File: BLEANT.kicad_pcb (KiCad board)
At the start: 4 copper layers, 75.8 x 76.2 mm, 71 parts, among them IC1 FAN4010IL6X_F113, IC2 FAN4010IL6X_F113, J1 Conn_01x04_Male, J2 SC_19-20, J3 Conn_01x02, J4 Conn_01x02, J5 1909763-1, U1 nRF51x22-QFxx, U2 LM50BIM3, U3 MP5077GG-Z, U4 MP5077GG-Z, U5 MCP2515-xSO, U6 SN65HVD1050D, X2 32.768kHz, Y1 16MHz

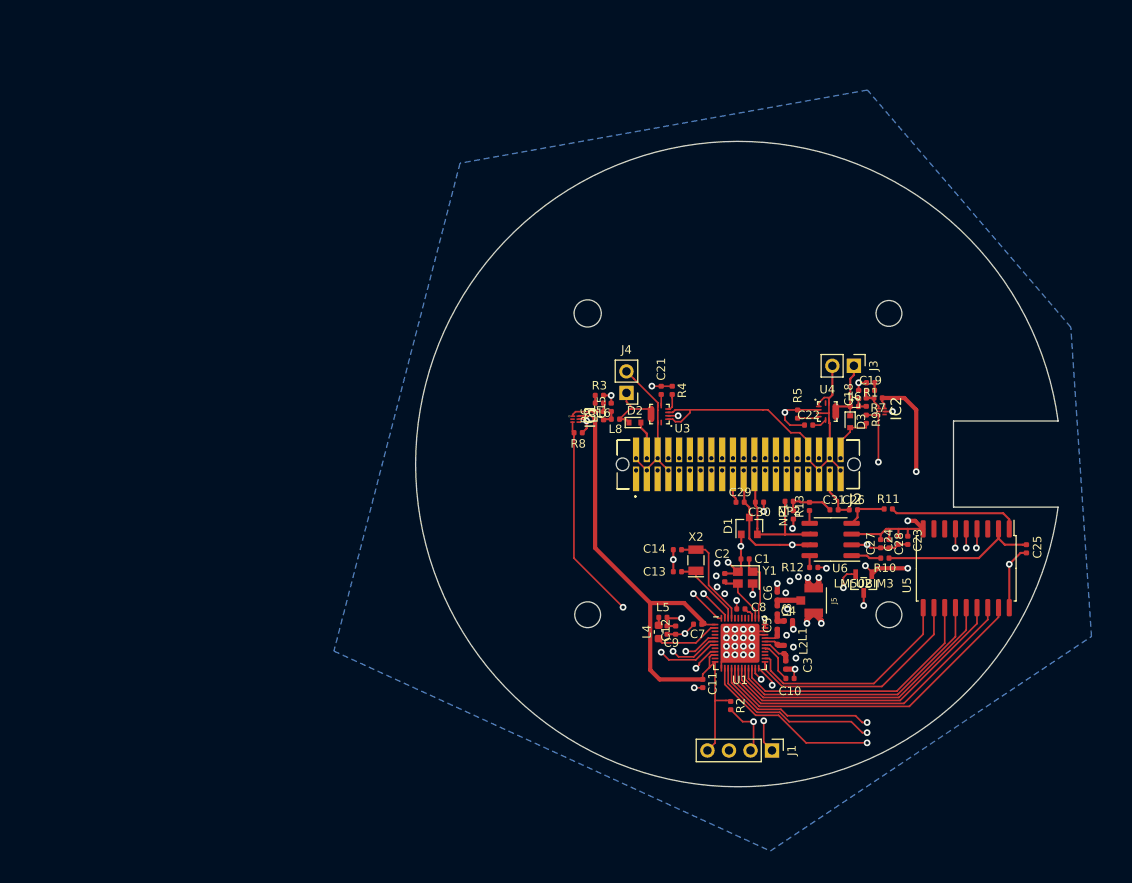
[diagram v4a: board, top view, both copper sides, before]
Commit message: Added ground pours and stitching vias
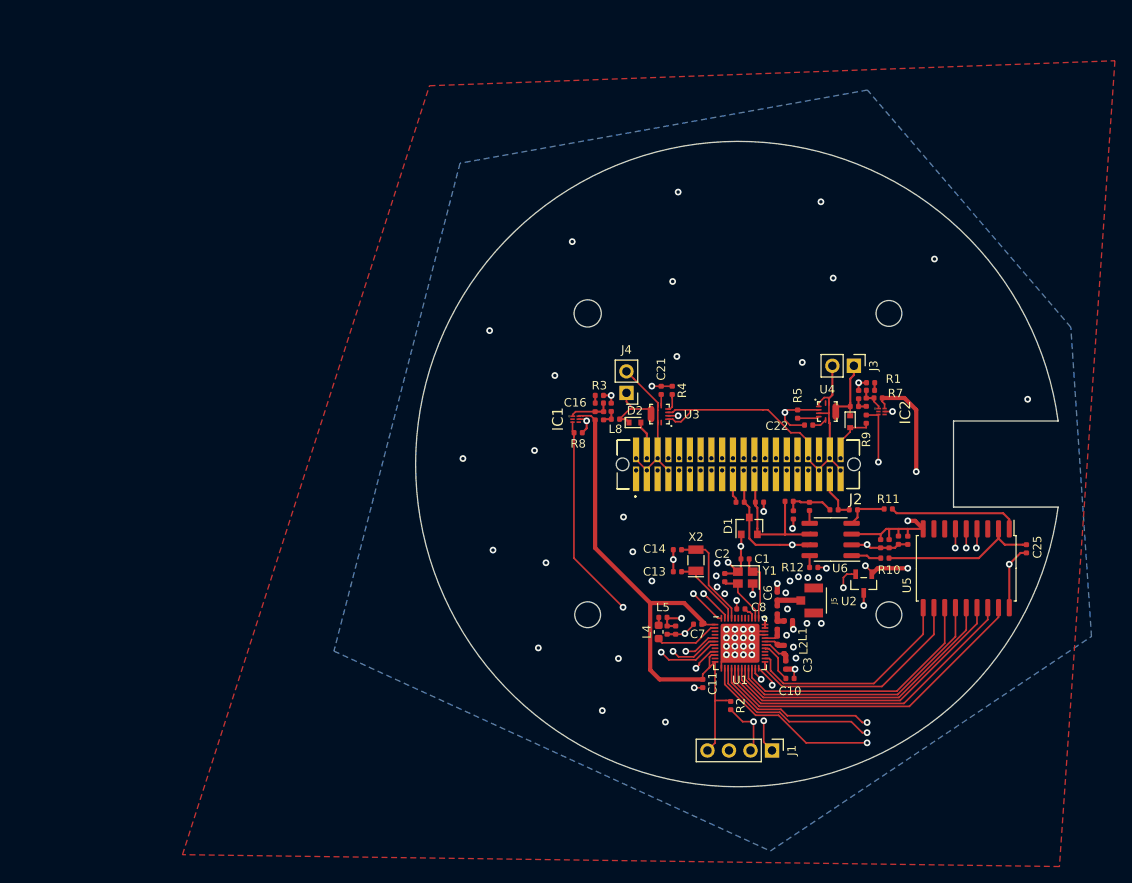
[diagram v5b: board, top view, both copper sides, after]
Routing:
- net GND: track 97.0 -> 90.9 mm, vias 53 -> 75
- added copper zone on F.Cu, net GND
- added copper zone on In2.Cu, net GND

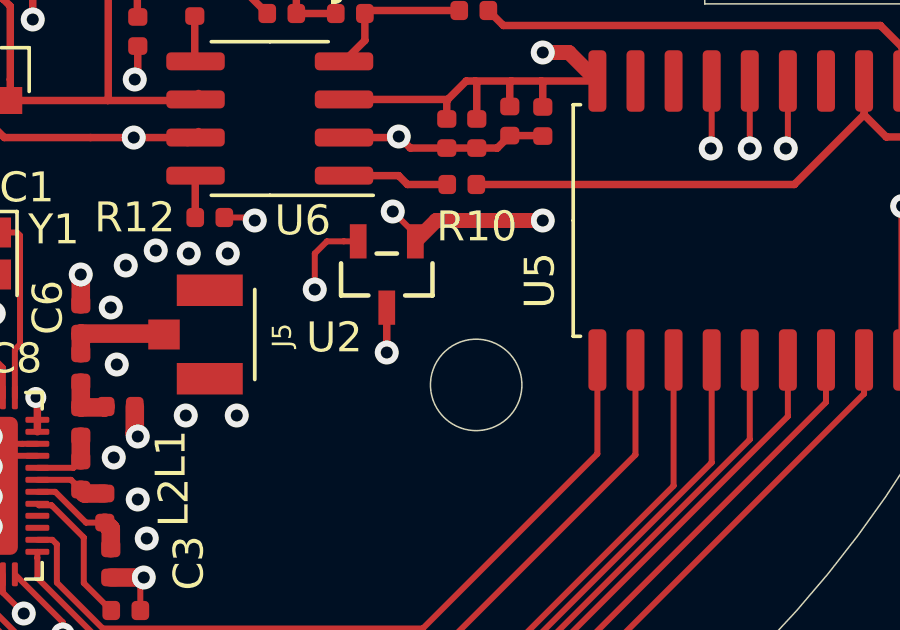
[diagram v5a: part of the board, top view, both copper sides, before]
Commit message: Made my chip not blow up with voltage dividers
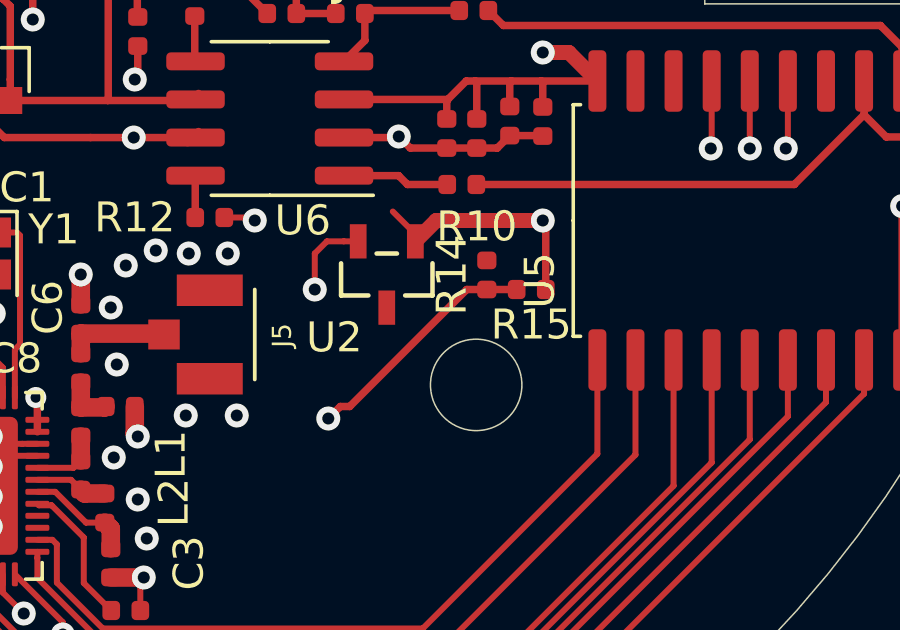
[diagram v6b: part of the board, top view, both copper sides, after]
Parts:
- added R14: 10k, Resistor_SMD:R_0402_1005Metric, F.Cu at (170.5, 141.1)
- added R15: 6k, Resistor_SMD:R_0402_1005Metric, F.Cu at (172.0, 141.6)
- C21: value 0.56uF -> 0.68uF
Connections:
- U1 pad 5: +5V -> Net-(R14-Pad1)
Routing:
- net Net-(R14-Pad1): track 0.00 -> 50.3 mm, vias 0 -> 2
- net +5V: track 95.1 -> 47.8 mm, vias 5 -> 3
- net GND: track 90.9 -> 89.4 mm, vias 75 -> 74
- net Temperature: track 45.0 -> 45.6 mm

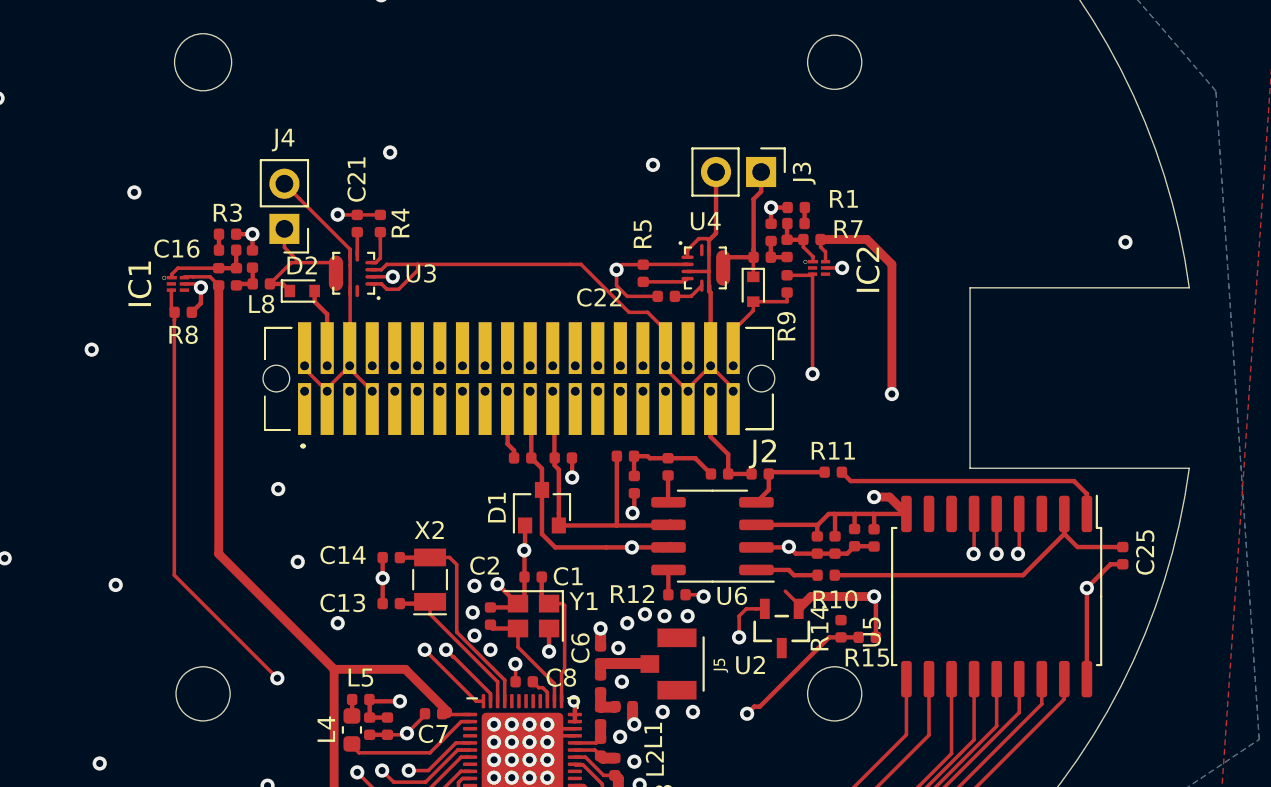
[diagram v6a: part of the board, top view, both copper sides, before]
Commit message: Changed filter and fixed CAN circuit
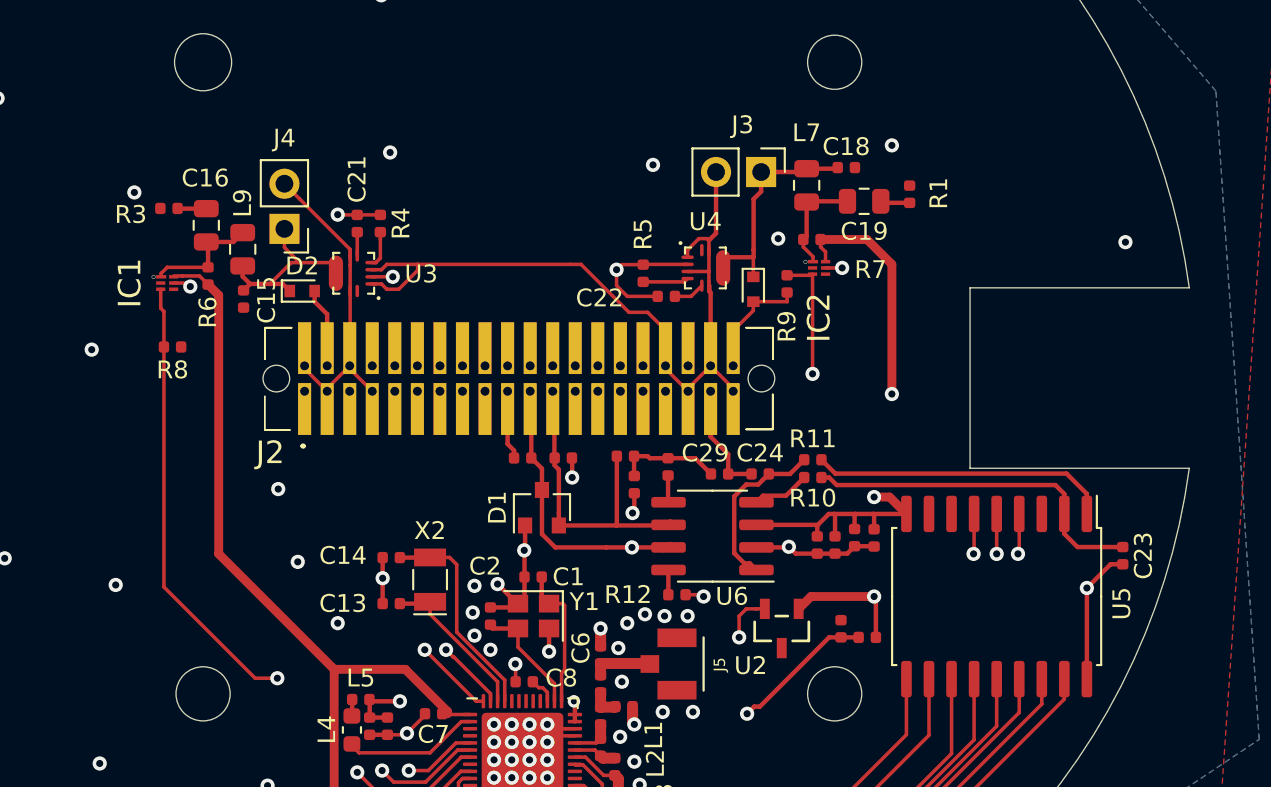
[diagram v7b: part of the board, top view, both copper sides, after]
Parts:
- removed L6, L8: 2.2uH, Inductor_SMD:L_0402_1005Metric
- C13, C14: value 21pF -> 20pF
- C16, C19: value 3.3uF -> 22uF; footprint Capacitor_SMD:C_0402_1005Metric -> Capacitor_SMD:C_0805_2012Metric
- L7, L9: value 1uH -> 4.7uH; footprint Inductor_SMD:L_0402_1005Metric -> Inductor_SMD:L_0805_2012Metric
- NP1, NP2: value 120 -> 60
- R1, R3: value 15 -> 1
- moved R1 6.43 mm to (174.4, 116.7), turned to 90 degrees
- moved C18 5.59 mm to (170.8, 115.2), turned to 0 degrees
- moved R10 5.55 mm to (168.9, 132.6)
- moved C19 4.04 mm to (171.8, 117.0)
- moved L7 3.72 mm to (168.6, 116.2), turned to 270 degrees
- moved R3 3.60 mm to (132.7, 117.5), turned to 180 degrees
- moved C15 2.30 mm to (136.9, 122.5), turned to 270 degrees
- moved R8 2.04 mm to (132.9, 125.2)
- moved C16 1.84 mm to (134.8, 118.4), turned to 90 degrees
- moved L9 1.59 mm to (136.8, 119.8)
- moved R11 1.35 mm to (168.9, 131.6)
- moved IC1 0.60 mm to (132.6, 121.7)
- moved R6 0.60 mm to (134.9, 121.2)
- renumbered C23 to C17, C24 to C20, C25 to C23, C26 to C24, C27 to C25, C28 to C26, C29 to C27, C30 to C28, C31 to C29
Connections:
- C24 pad 2: Net-(C26-Pad2) -> Net-(C24-Pad2)
- D2 pad 1: Net-(D2-Pad1) -> Net-(C15-Pad1)
- D3 pad 1: Net-(D3-Pad1) -> Net-(C18-Pad1)
- J3 pad 1: Net-(D3-Pad1) -> Net-(C18-Pad1)
- J4 pad 1: Net-(D2-Pad1) -> Net-(C15-Pad1)
- R11 pad 1: Net-(C26-Pad2) -> Net-(C24-Pad2)
- U3 pad 10: Net-(D2-Pad1) -> Net-(C15-Pad1)
- U3 pad 7: Net-(D2-Pad1) -> Net-(C15-Pad1)
- U3 pad 8: Net-(D2-Pad1) -> Net-(C15-Pad1)
- U3 pad 9: Net-(D2-Pad1) -> Net-(C15-Pad1)
- U4 pad 10: Net-(D3-Pad1) -> Net-(C18-Pad1)
- U4 pad 7: Net-(D3-Pad1) -> Net-(C18-Pad1)
- U4 pad 8: Net-(D3-Pad1) -> Net-(C18-Pad1)
- U4 pad 9: Net-(D3-Pad1) -> Net-(C18-Pad1)
- U6 pad 1: Net-(R10-Pad2) -> Net-(C24-Pad2)
- U6 pad 4: Net-(C26-Pad2) -> Net-(R10-Pad2)
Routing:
- net Net-(C18-Pad1): track 1.85 -> 13.4 mm
- net Net-(C15-Pad1): track 1.87 -> 11.8 mm
- net Net-(C24-Pad2): track 0.00 -> 9.77 mm
- net Net-(D3-Pad1): track 9.00 -> 0.00 mm
- net Net-(D2-Pad1): track 8.94 -> 0.00 mm
- net GND: track 89.4 -> 84.1 mm
- net Net-(C26-Pad2): track 5.07 -> 0.00 mm
- net Net-(C19-Pad1): track 3.27 -> 5.95 mm
- net Net-(C16-Pad1): track 4.87 -> 6.68 mm
- net Net-(R11-Pad2): track 15.4 -> 16.9 mm
- net Net-(C23-Pad1): track 18.6 -> 19.9 mm
- net +5V: track 47.8 -> 46.8 mm
- net 3V3Sense: track 39.7 -> 40.7 mm
- net Net-(C19-Pad2): track 0.91 -> 1.66 mm
- net Net-(C16-Pad2): track 0.90 -> 1.62 mm
